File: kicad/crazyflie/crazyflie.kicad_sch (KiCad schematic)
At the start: 16 parts, among them J1 Conn_01x04_Socket, J2 Conn_01x03_Socket, J3 Conn_01x02_Socket, J4 Conn_01x14_Socket, J5 Conn_01x14_Socket, J6 Conn_01x04_Socket, J7 Conn_01x03_Socket, J8 Conn_01x04_Socket, M1 Conn_01x03_Socket, M2 Conn_01x03_Socket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

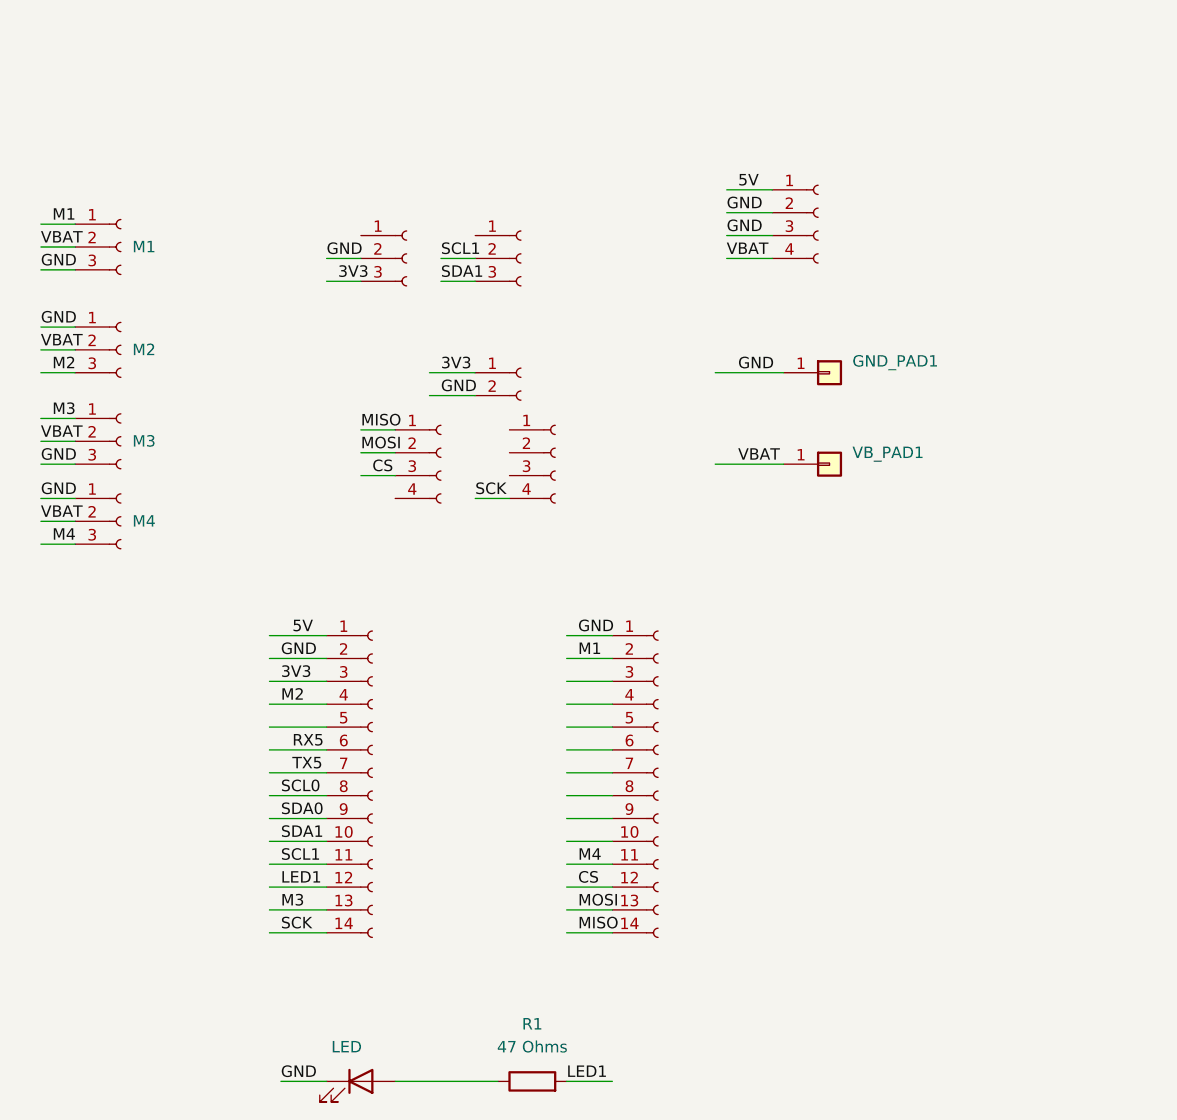
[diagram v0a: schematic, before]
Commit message: modified:   kicad/crazyflie/crazyflie.kicad_pro
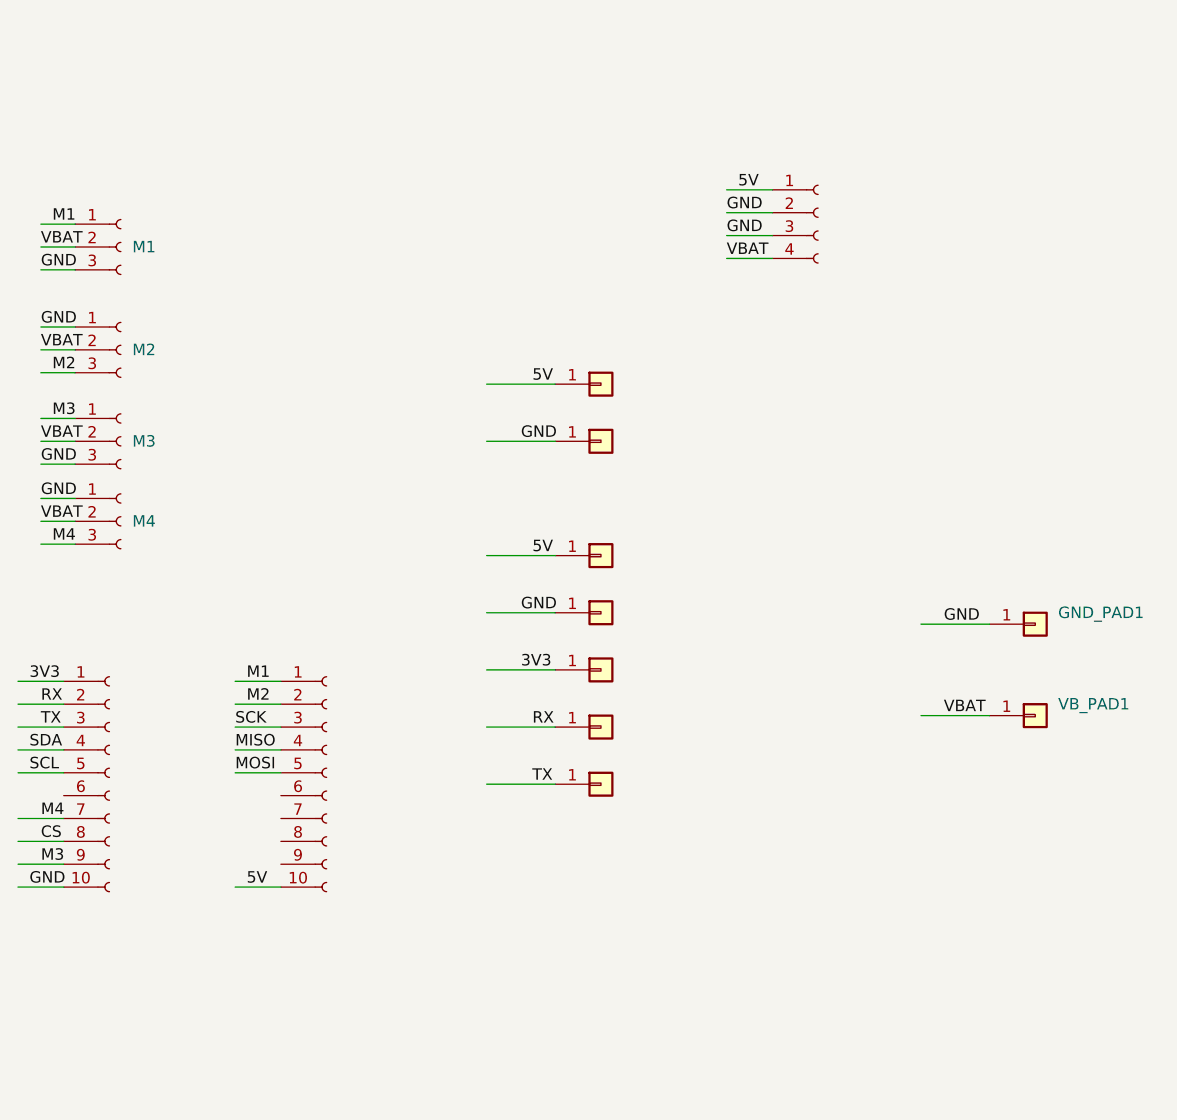
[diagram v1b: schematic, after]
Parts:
- removed D1: LED, LED_THT:LED_D3.0mm, symbol Device:LED
- removed J1, J6: Conn_01x04_Socket, Connector_PinSocket_2.54mm:PinSocket_1x04_P2.54mm_Vertical, symbol Connector:Conn_01x04_Socket
- removed J2, J7: Conn_01x03_Socket, Connector_PinSocket_2.54mm:PinSocket_1x03_P2.54mm_Vertical, symbol Connector:Conn_01x03_Socket
- removed J3: Conn_01x02_Socket, Connector_PinSocket_2.54mm:PinSocket_1x02_P2.54mm_Vertical, symbol Connector:Conn_01x02_Socket
- removed J4, J5: Conn_01x14_Socket, Connector_PinSocket_2.54mm:PinSocket_1x14_P2.54mm_Vertical, symbol Connector:Conn_01x14_Socket
- removed R1: 47 Ohms, Resistor_THT:R_Axial_DIN0204_L3.6mm_D1.6mm_P5.08mm_Horizontal, symbol Device:R
- added J1, J2: Conn_01x10_Female, Connector_PinHeader_2.00mm:PinHeader_1x10_P2.00mm_Vertical, symbol Connector:Conn_01x10_Female
- added VB_PAD10, VB_PAD11, VB_PAD12, VB_PAD5, VB_PAD6, VB_PAD8, VB_PAD9: Conn_01x01, Connector_Wire:SolderWirePad_1x01_SMD_1x2mm, symbol Connector_Generic:Conn_01x01
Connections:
- net 3V3: now also J1.1 (Pin_1), VB_PAD10.1 (Pin_1)
- net 5V: now also J2.10 (Pin_10), VB_PAD11.1 (Pin_1), VB_PAD8.1 (Pin_1)
- net CS: now also J1.8 (Pin_8)
- net GND: now also J1.10 (Pin_10), VB_PAD12.1 (Pin_1), VB_PAD9.1 (Pin_1)
- net M1: now also J2.1 (Pin_1)
- net M2: now also J2.2 (Pin_2)
- net M3: now also J1.9 (Pin_9)
- net M4: now also J1.7 (Pin_7)
- net MISO: now also J2.4 (Pin_4)
- net MOSI: now also J2.5 (Pin_5)
- net SCK: now also J2.3 (Pin_3)
- new net RX: J1.2 (Pin_2), VB_PAD5.1 (Pin_1)
- new net SCL: J1.5 (Pin_5)
- new net SDA: J1.4 (Pin_4)
- new net TX: J1.3 (Pin_3), VB_PAD6.1 (Pin_1)
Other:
- moved on the sheet: GND_PAD1, VB_PAD1

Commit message: modified:   kicad/crazyflie/crazyflie.kicad_pcb
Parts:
- removed GND_PAD1, VB_PAD1: Conn_01x01, Connector_Wire:SolderWirePad_1x01_SMD_5x10mm, symbol Connector_Generic:Conn_01x01
- removed VB_PAD10, VB_PAD11, VB_PAD12, VB_PAD5, VB_PAD6, VB_PAD8, VB_PAD9: Conn_01x01, Connector_Wire:SolderWirePad_1x01_SMD_1x2mm, symbol Connector_Generic:Conn_01x01

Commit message: modified:   kicad/crazyflie/crazyflie.kicad_pcb
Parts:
- added H1: MountingHole, MountingHole:MountingHole_5.3mm_M5_ISO7380_Pad_TopOnly, symbol Mechanical:MountingHole
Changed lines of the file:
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@@
+	)
+	(symbol
+		(lib_id "Mechanical:MountingHole")
+		(at 166.37 58.42 0)
+		(unit 1)
+		(exclude_from_sim no)
+		(in_bom no)
+		(on_board yes)
+		(dnp no)
+		(fields_autoplaced yes)
+		(property "Reference" "H1"
+			(at 168.91 57.1499 0)
+			(effects
+				(font
+					(size 1.27 1.27)
+				)
+				(justify left)
+			)
+		)
+		(property "Value" "MountingHole"
+			(at 168.91 59.6899 0)
+			(effects
+				(font
+					(size 1.27 1.27)
+				)
+				(justify left)
+			)
+		)
+		(property "Footprint" "MountingHole:MountingHole_5.3mm_M5_ISO7380_Pad_TopOnly"
+			(at 166.37 58.42 0)
+			(effects
+				(font
+					(size 1.27 1.27)
+				)
+				(hide yes)
+			)
+		)
+		(property "Datasheet" "~"
+			(at 166.37 58.42 0)
+			(effects
+				(font
+					(size 1.27 1.27)
+				)
+				(hide yes)
+			)
+		)
+		(property "Description" "Mounting Hole without connection"
+			(at 166.37 58.42 0)
+			(effects
+				(font
+					(size 1.27 1.27)
+				)
+				(hide yes)
+			)
+		)
+		(instances
+			(project ""
+				(path "/afb8e687-4a13-41a1-b8c0-89a749e897fe"
+					(reference "H1")
+					(unit 1)
+				)
+			)
+		)
 	)
 	(symbol

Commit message: modified:   kicad/crazyflie/crazyflie.kicad_pcb
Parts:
- removed H1: MountingHole, MountingHole:MountingHole_5.3mm_M5_ISO7380_Pad_TopOnly, symbol Mechanical:MountingHole
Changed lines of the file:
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@@
-	)
-	(symbol
-		(lib_id "Mechanical:MountingHole")
-		(at 166.37 58.42 0)
-		(unit 1)
-		(exclude_from_sim no)
-		(in_bom no)
-		(on_board yes)
-		(dnp no)
-		(fields_autoplaced yes)
-		(property "Reference" "H1"
-			(at 168.91 57.1499 0)
-			(effects
-				(font
-					(size 1.27 1.27)
-				)
-				(justify left)
-			)
-		)
-		(property "Value" "MountingHole"
-			(at 168.91 59.6899 0)
-			(effects
-				(font
-					(size 1.27 1.27)
-				)
-				(justify left)
-			)
-		)
-		(property "Footprint" "MountingHole:MountingHole_5.3mm_M5_ISO7380_Pad_TopOnly"
-			(at 166.37 58.42 0)
-			(effects
-				(font
-					(size 1.27 1.27)
-				)
-				(hide yes)
-			)
-		)
-		(property "Datasheet" "~"
-			(at 166.37 58.42 0)
-			(effects
-				(font
-					(size 1.27 1.27)
-				)
-				(hide yes)
-			)
-		)
-		(property "Description" "Mounting Hole without connection"
-			(at 166.37 58.42 0)
-			(effects
-				(font
-					(size 1.27 1.27)
-				)
-				(hide yes)
-			)
-		)
-		(instances
-			(project ""
-				(path "/afb8e687-4a13-41a1-b8c0-89a749e897fe"
-					(reference "H1")
-					(unit 1)
-				)
-			)
-		)
 	)
 	(symbol
